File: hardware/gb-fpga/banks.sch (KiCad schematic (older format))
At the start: 1 part, among them U1 xc7s25ftgb196

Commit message: Connect flash config circuit
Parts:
- removed U1: xc7s25ftgb196, Package_BGA:Xilinx_FTGB196, symbol xilinx7:xc7s25ftgb196
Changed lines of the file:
@@
 $Descr A4 11693 8268
 encoding utf-8
-Sheet 4 6
+Sheet 3 6
 Title "Banks"
 Date ""
@@
 Comment4 ""
 $EndDescr
-$Comp
-L xilinx7:xc7s25ftgb196 U1
-U 2 1 60CF46E4
-P 2800 1300
-F 0 "U1" H 4531 -1147 60  0000 L CNN
-F 1 "xc7s25ftgb196" H 4531 -1253 60  0000 L CNN
-F 2 "Package_BGA:Xilinx_FTGB196" H 3000 1350 60  0001 L CNN
-F 3 "" H 3000 1150 60  0001 L CNN
-F 4 "xc7s25ftgb196" H 3000 1050 60  0001 L CNN "desc"
-	2    2800 1300
-	1    0    0    -1
-$EndComp
-$Comp
-L xilinx7:xc7s25ftgb196 U1
-U 3 1 60CF7DA5
-P 7000 1250
-F 0 "U1" H 8231 -1197 60  0000 L CNN
-F 1 "xc7s25ftgb196" H 8231 -1303 60  0000 L CNN
-F 2 "Package_BGA:Xilinx_FTGB196" H 7200 1300 60  0001 L CNN
-F 3 "" H 7200 1100 60  0001 L CNN
-F 4 "xc7s25ftgb196" H 7200 1000 60  0001 L CNN "desc"
-	3    7000 1250
-	1    0    0    -1
-$EndComp
 $EndSCHEMATC

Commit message: Add USB connections
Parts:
- added U1: xc7s25ftgb196, symbol gb-fpga:xc7s25ftgb196
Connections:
- new net RX: U1.F1 (IO_L9N_T1_DQS_34)
- new net TX: U1.G1 (IO_L9P_T1_DQS_34)
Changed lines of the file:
@@
 Comment4 ""
 $EndDescr
+$Comp
+L gb-fpga:xc7s25ftgb196 U1
+U 2 1 60E62F9D
+P 2900 1750
+F 0 "U1" H 4628 -297 60  0000 L CNN
+F 1 "xc7s25ftgb196" H 4628 -403 60  0000 L CNN
+F 2 "" H 3100 1800 60  0001 L CNN
+F 3 "" H 3100 1600 60  0001 L CNN
+	2    2900 1750
+	1    0    0    -1
+$EndComp
+$Comp
+L gb-fpga:xc7s25ftgb196 U1
+U 3 1 60E6F7B8
+P 7150 1150
+F 0 "U1" H 8378 -1247 60  0000 L CNN
+F 1 "xc7s25ftgb196" H 8378 -1353 60  0000 L CNN
+F 2 "" H 7350 1200 60  0001 L CNN
+F 3 "" H 7350 1000 60  0001 L CNN
+	3    7150 1150
+	1    0    0    -1
+$EndComp
+Wire Wire Line
+	7150 2950 7000 2950
+Wire Wire Line
+	7150 3050 7000 3050
+Text GLabel 7000 2950 0    50   Output ~ 0
+RX
+Text GLabel 7000 3050 0    50   Input ~ 0
+TX
 $EndSCHEMATC

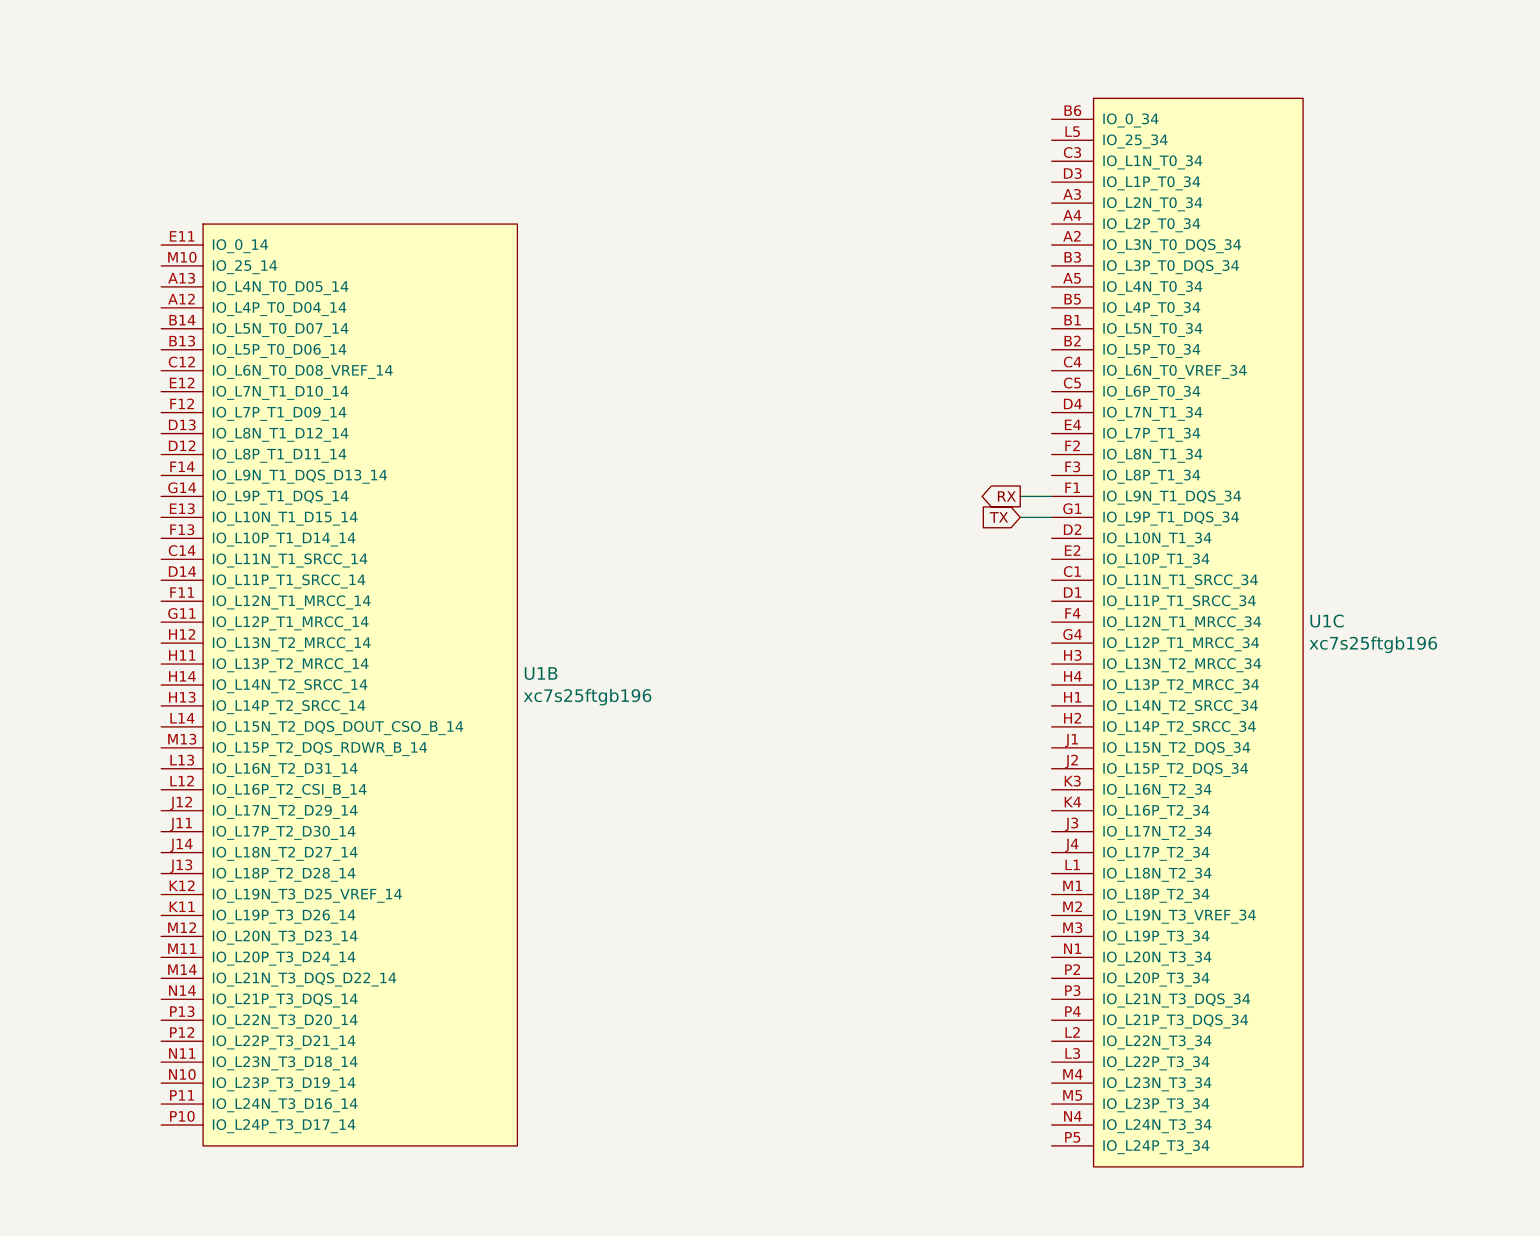
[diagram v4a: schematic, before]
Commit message: Add oscillator
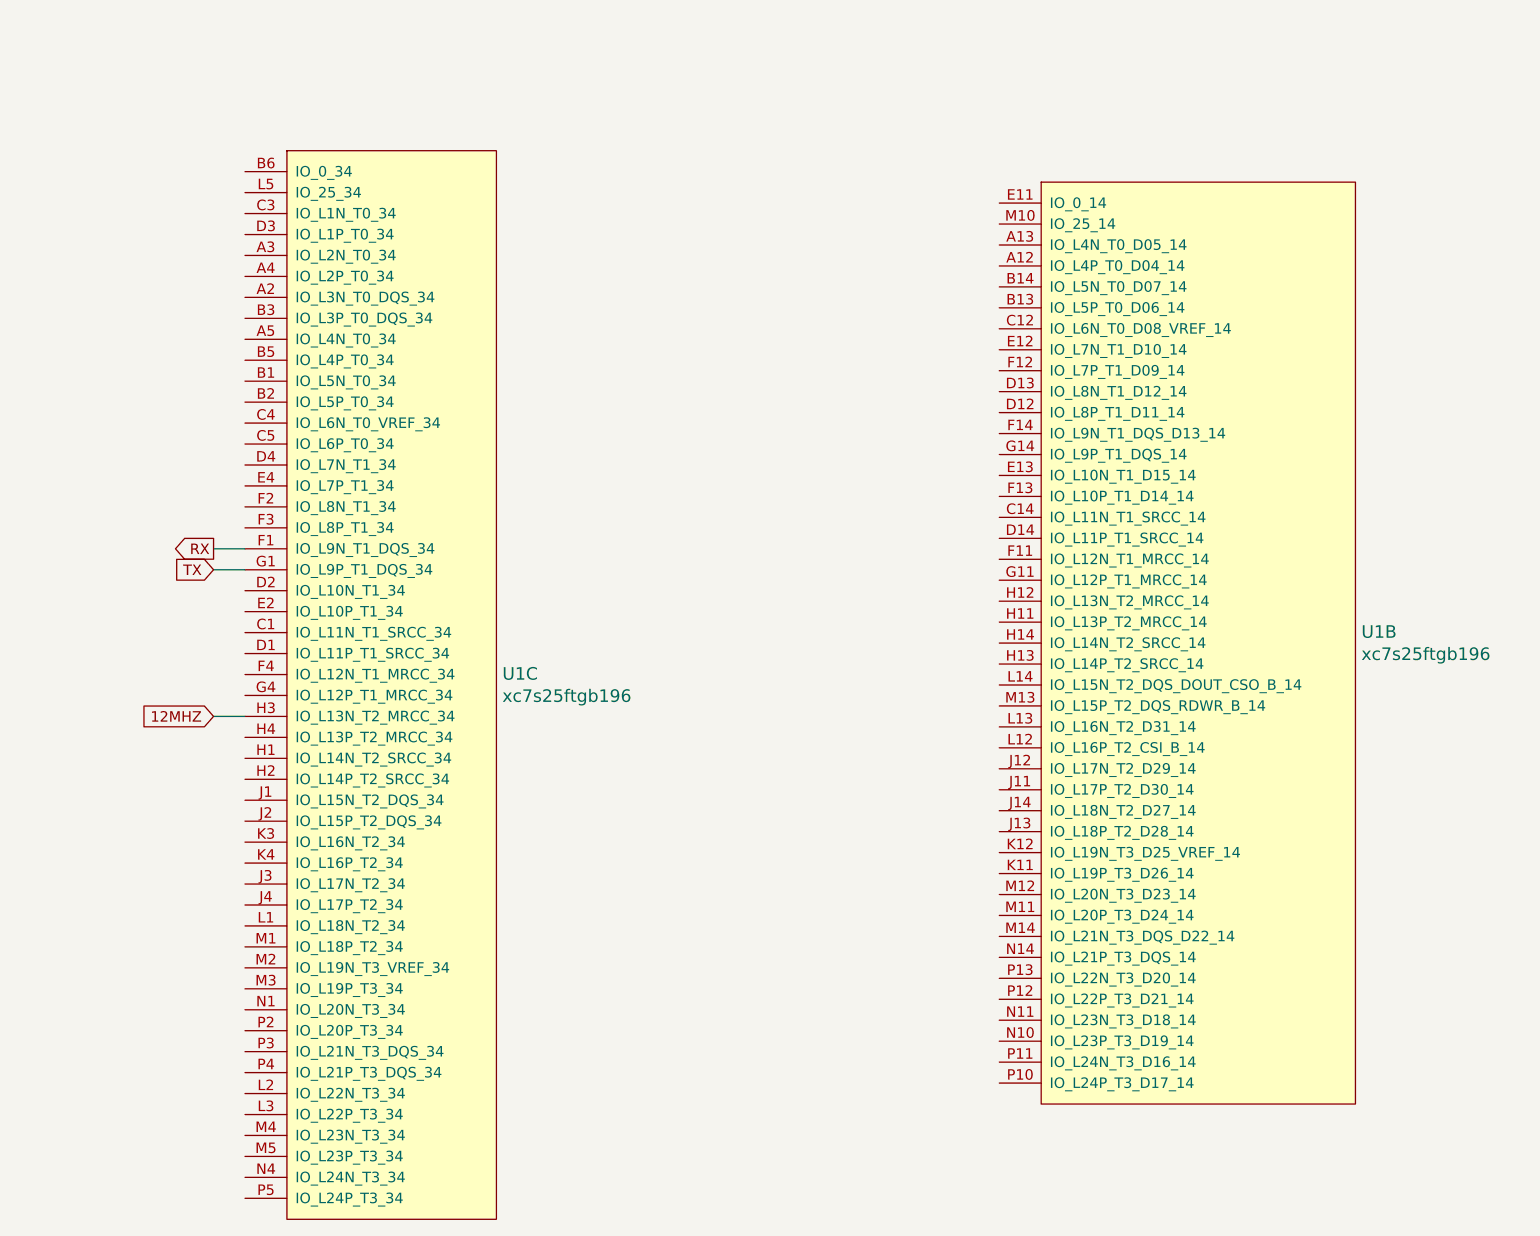
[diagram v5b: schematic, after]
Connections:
- net 12MHZ: now reaches U1.H3 (IO_L13N_T2_MRCC_34)
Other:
- moved on the sheet: U1B, U1C
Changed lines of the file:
@@
 L gb-fpga:xc7s25ftgb196 U1
 U 2 1 60E62F9D
-P 2900 1750
-F 0 "U1" H 4628 -297 60  0000 L CNN
-F 1 "xc7s25ftgb196" H 4628 -403 60  0000 L CNN
-F 2 "" H 3100 1800 60  0001 L CNN
-F 3 "" H 3100 1600 60  0001 L CNN
-	2    2900 1750
+P 6900 1550
+F 0 "U1" H 8628 -497 60  0000 L CNN
+F 1 "xc7s25ftgb196" H 8628 -603 60  0000 L CNN
+F 2 "" H 7100 1600 60  0001 L CNN
+F 3 "" H 7100 1400 60  0001 L CNN
+	2    6900 1550
 	1    0    0    -1
 $EndComp
@@
 L gb-fpga:xc7s25ftgb196 U1
 U 3 1 60E6F7B8
-P 7150 1150
-F 0 "U1" H 8378 -1247 60  0000 L CNN
-F 1 "xc7s25ftgb196" H 8378 -1353 60  0000 L CNN
-F 2 "" H 7350 1200 60  0001 L CNN
-F 3 "" H 7350 1000 60  0001 L CNN
-	3    7150 1150
+P 3300 1400
+F 0 "U1" H 4528 -997 60  0000 L CNN
+F 1 "xc7s25ftgb196" H 4528 -1103 60  0000 L CNN
+F 2 "" H 3500 1450 60  0001 L CNN
+F 3 "" H 3500 1250 60  0001 L CNN
+	3    3300 1400
 	1    0    0    -1
 $EndComp
 Wire Wire Line
-	7150 2950 7000 2950
+	3300 3200 3150 3200
 Wire Wire Line
-	7150 3050 7000 3050
-Text GLabel 7000 2950 0    50   Output ~ 0
+	3300 3300 3150 3300
+Text GLabel 3150 3200 0    50   Output ~ 0
 RX
-Text GLabel 7000 3050 0    50   Input ~ 0
+Text GLabel 3150 3300 0    50   Input ~ 0
 TX
+Wire Wire Line
+	3300 4000 3150 4000
+Text GLabel 3150 4000 0    50   Input ~ 0
+12MHZ
 $EndSCHEMATC

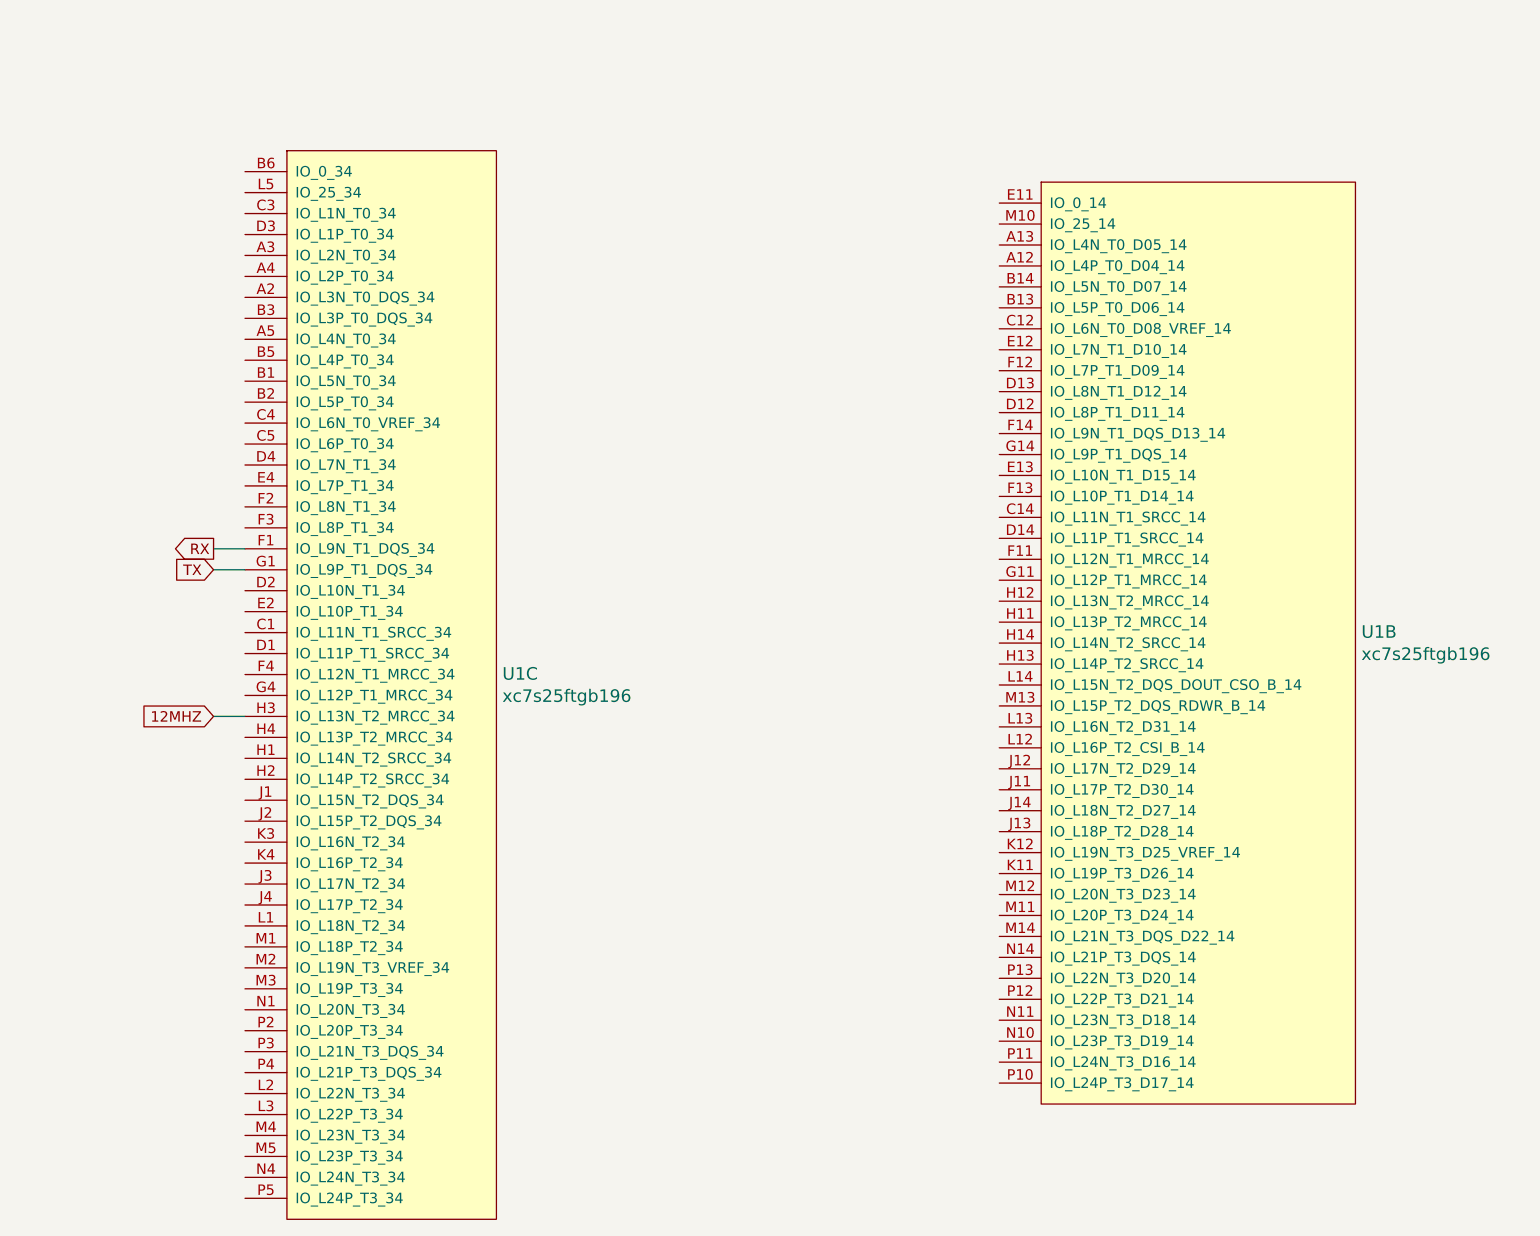
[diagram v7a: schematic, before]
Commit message: Assign cartridge pins to fpga
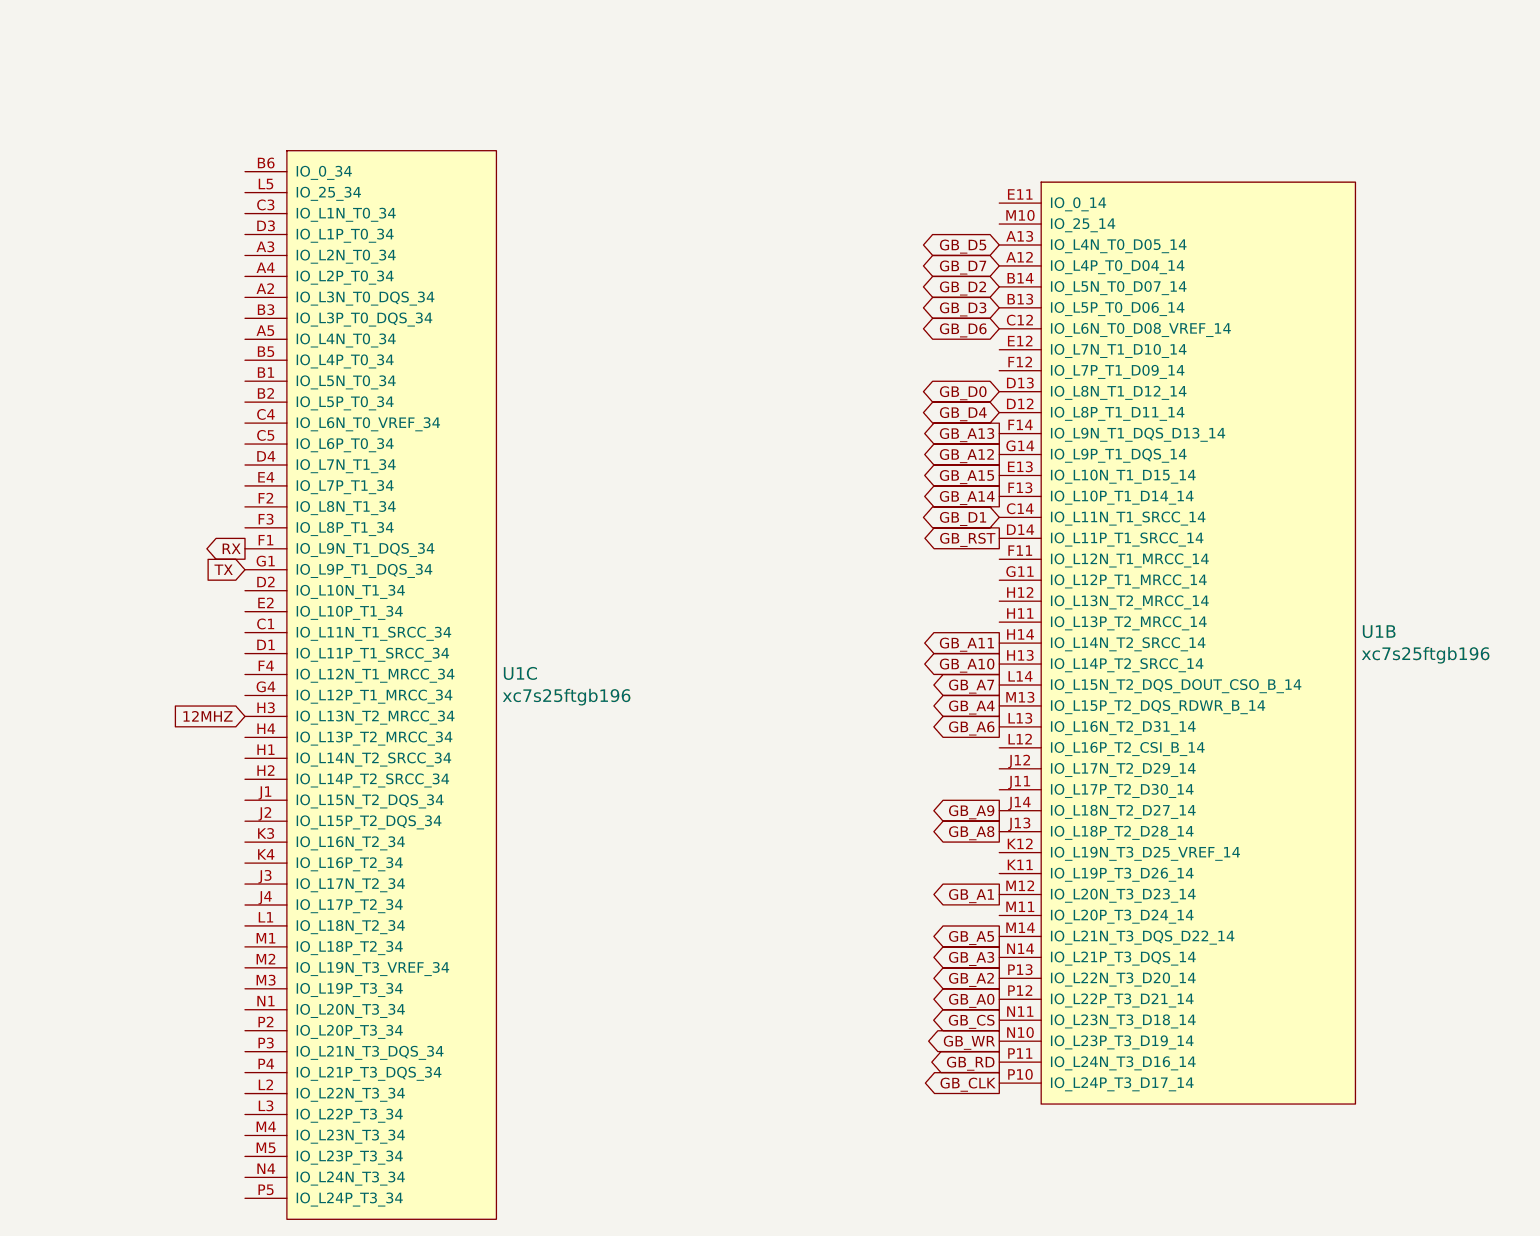
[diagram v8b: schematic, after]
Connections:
- net GB_D7: now reaches U1.A12 (IO_L4P_T0_D04_14)
- net GB_D5: now reaches U1.A13 (IO_L4N_T0_D05_14)
- net GB_D3: now reaches U1.B13 (IO_L5P_T0_D06_14)
- net GB_D2: now reaches U1.B14 (IO_L5N_T0_D07_14)
- net GB_D6: now reaches U1.C12 (IO_L6N_T0_D08_VREF_14)
- net GB_D1: now reaches U1.C14 (IO_L11N_T1_SRCC_14)
- net GB_D4: now reaches U1.D12 (IO_L8P_T1_D11_14)
- net GB_D0: now reaches U1.D13 (IO_L8N_T1_D12_14)
- net GB_RST: now reaches U1.D14 (IO_L11P_T1_SRCC_14)
- net GB_A15: now reaches U1.E13 (IO_L10N_T1_D15_14)
- net GB_A14: now reaches U1.F13 (IO_L10P_T1_D14_14)
- net GB_A13: now reaches U1.F14 (IO_L9N_T1_DQS_D13_14)
- net GB_A12: now reaches U1.G14 (IO_L9P_T1_DQS_14)
- net GB_A10: now reaches U1.H13 (IO_L14P_T2_SRCC_14)
- net GB_A11: now reaches U1.H14 (IO_L14N_T2_SRCC_14)
- net GB_A8: now reaches U1.J13 (IO_L18P_T2_D28_14)
- net GB_A9: now reaches U1.J14 (IO_L18N_T2_D27_14)
- net GB_A6: now reaches U1.L13 (IO_L16N_T2_D31_14)
- net GB_A7: now reaches U1.L14 (IO_L15N_T2_DQS_DOUT_CSO_B_14)
- net GB_A1: now reaches U1.M12 (IO_L20N_T3_D23_14)
- net GB_A4: now reaches U1.M13 (IO_L15P_T2_DQS_RDWR_B_14)
- net GB_A5: now reaches U1.M14 (IO_L21N_T3_DQS_D22_14)
- net GB_WR: now reaches U1.N10 (IO_L23P_T3_D19_14)
- net GB_CS: now reaches U1.N11 (IO_L23N_T3_D18_14)
- net GB_A3: now reaches U1.N14 (IO_L21P_T3_DQS_14)
- net GB_CLK: now reaches U1.P10 (IO_L24P_T3_D17_14)
- net GB_RD: now reaches U1.P11 (IO_L24N_T3_D16_14)
- net GB_A0: now reaches U1.P12 (IO_L22P_T3_D21_14)
- net GB_A2: now reaches U1.P13 (IO_L22N_T3_D20_14)
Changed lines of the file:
@@
 	1    0    0    -1
 $EndComp
-Wire Wire Line
-	3300 3200 3150 3200
-Wire Wire Line
-	3300 3300 3150 3300
-Text GLabel 3150 3200 0    50   Output ~ 0
+Text GLabel 3300 3200 0    50   Output ~ 0
 RX
-Text GLabel 3150 3300 0    50   Input ~ 0
+Text GLabel 3300 3300 0    50   Input ~ 0
 TX
-Wire Wire Line
-	3300 4000 3150 4000
-Text GLabel 3150 4000 0    50   Input ~ 0
+Text GLabel 3300 4000 0    50   Input ~ 0
 12MHZ
+Text GLabel 6900 5750 0    50   Output ~ 0
+GB_CLK
+Text GLabel 6900 5550 0    50   Output ~ 0
+GB_WR
+Text GLabel 6900 5650 0    50   Output ~ 0
+GB_RD
+Text GLabel 6900 5450 0    50   Output ~ 0
+GB_CS
+Text GLabel 6900 5350 0    50   Output ~ 0
+GB_A0
+Text GLabel 6900 4850 0    50   Output ~ 0
+GB_A1
+Text GLabel 6900 5250 0    50   Output ~ 0
+GB_A2
+Text GLabel 6900 5150 0    50   Output ~ 0
+GB_A3
+Text GLabel 6900 3950 0    50   Output ~ 0
+GB_A4
+Text GLabel 6900 5050 0    50   Output ~ 0
+GB_A5
+Text GLabel 6900 4050 0    50   Output ~ 0
+GB_A6
+Text GLabel 6900 3850 0    50   Output ~ 0
+GB_A7
+Text GLabel 6900 4550 0    50   Output ~ 0
+GB_A8
+Text GLabel 6900 4450 0    50   Output ~ 0
+GB_A9
+Text GLabel 6900 3750 0    50   Output ~ 0
+GB_A10
+Text GLabel 6900 3650 0    50   Output ~ 0
+GB_A11
+Text GLabel 6900 2750 0    50   Output ~ 0
+GB_A12
+Text GLabel 6900 2650 0    50   Output ~ 0
+GB_A13
+Text GLabel 6900 2950 0    50   Output ~ 0
+GB_A14
+Text GLabel 6900 2850 0    50   Output ~ 0
+GB_A15
+Text GLabel 6900 3150 0    50   Output ~ 0
+GB_RST
+Text GLabel 6900 2450 0    50   BiDi ~ 0
+GB_D0
+Text GLabel 6900 3050 0    50   BiDi ~ 0
+GB_D1
+Text GLabel 6900 1950 0    50   BiDi ~ 0
+GB_D2
+Text GLabel 6900 2050 0    50   BiDi ~ 0
+GB_D3
+Text GLabel 6900 2550 0    50   BiDi ~ 0
+GB_D4
+Text GLabel 6900 1750 0    50   BiDi ~ 0
+GB_D5
+Text GLabel 6900 2150 0    50   BiDi ~ 0
+GB_D6
+Text GLabel 6900 1850 0    50   BiDi ~ 0
+GB_D7
 $EndSCHEMATC
